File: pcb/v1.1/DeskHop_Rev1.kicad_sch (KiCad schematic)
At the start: 20 parts, among them J1 Keyboard In, J2 Debug2, J3 Debug1, J4 Mouse In, U2 Pico Primary Custom, U3 TPD4E1U06DBVR, U4 ADuM1201BR, U5 TPD4E1U06DBVR, U6 Pico Primary Custom

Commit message: ver OneXeroOne
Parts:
- removed J2: Debug2, Connector_PinHeader_2.54mm:PinHeader_1x03_P2.54mm_Vertical, symbol Connector_Generic:Conn_01x03
- removed J3: Debug1, Connector_PinHeader_2.54mm:PinHeader_1x03_P2.54mm_Vertical, symbol Connector_Generic:Conn_01x03
- removed U3: TPD4E1U06DBVR, Library:TPD4E1U06DBVR, symbol TPD4E1U06DBVR:TPD4E1U06DBVR
- added U1: TPD4E1U06DBVR, Customs:DBV6_TEX, symbol TPD4E1U06DBVR:TPD4E1U06DBVR
- U5: footprint Library:TPD4E1U06DBVR -> Customs:DBV6_TEX
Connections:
- net GND is gone; now on net GND2: H1.1
- net GND1: now also H2.1
- net GND2: now also U1.2 (GND); no longer H2.1
- net OA+: now also U1.1 (D1+), U1.3 (D2+)
- net OA-: now also U1.4 (D2-), U1.6 (D1-)
- net UART A RX: now also U6.14 (GPIO12); no longer U6.18 (GPIO15)
- net UART A TX: now also U6.13 (GPIO11); no longer U6.17 (GPIO14)
- net UART B RX: now also U2.27 (GPIO24); no longer U2.22 (GPIO19)
- net UART B TX: now also U2.26 (GPIO23); no longer U2.21 (GPIO18)

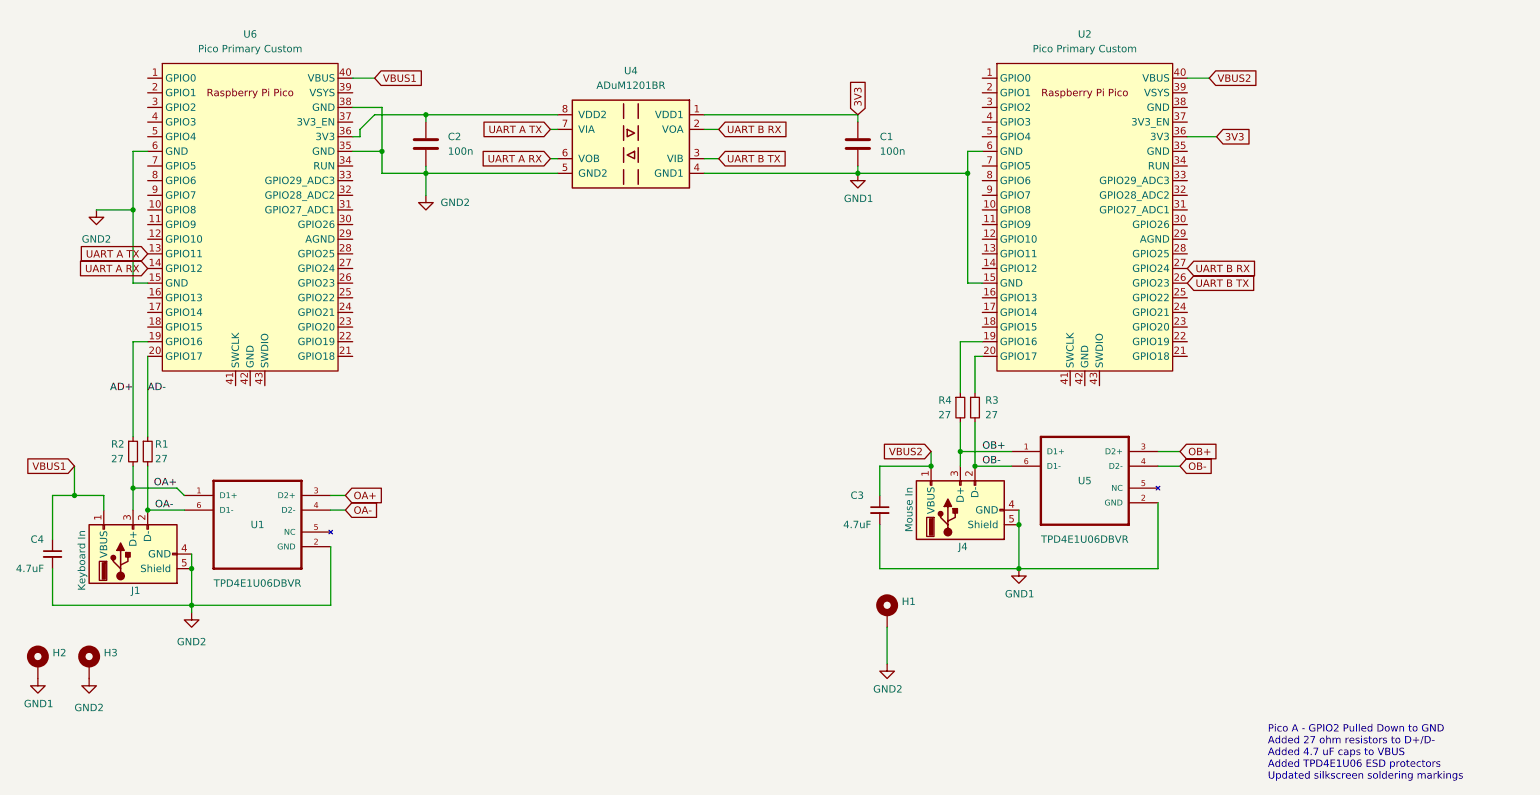
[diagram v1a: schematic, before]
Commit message: match pins to original board
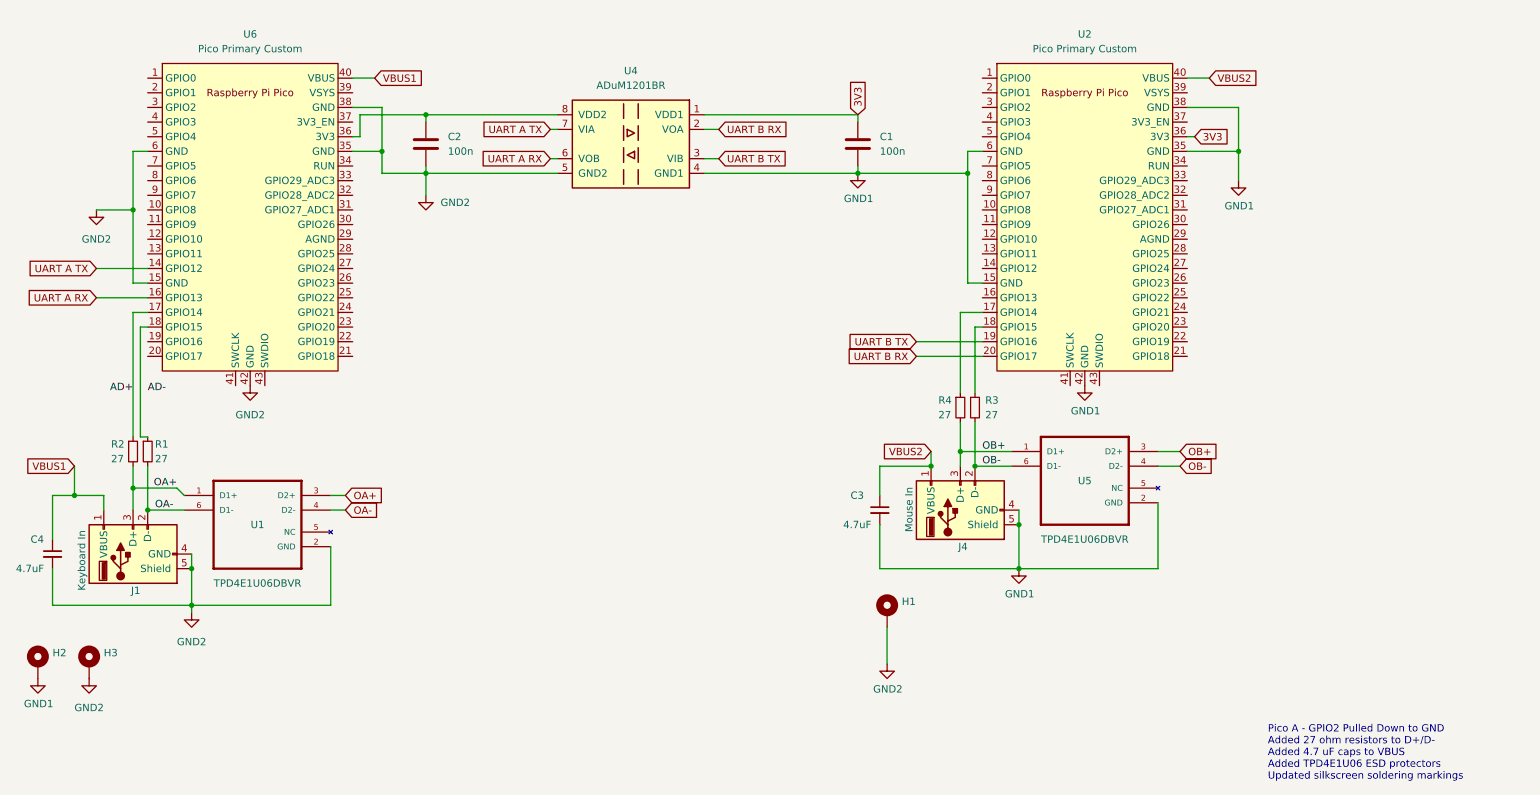
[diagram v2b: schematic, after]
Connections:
- net AD+: now also U6.17 (GPIO14); no longer U6.19 (GPIO16)
- net AD-: no longer R1.1, U6.20 (GPIO17)
- net GND1: now also U2.35 (GND), U2.38 (GND), U2.42 (GND)
- net GND2: now also U6.42 (GND)
- net UART A RX: now also U6.16 (GPIO13); no longer U6.14 (GPIO12)
- net UART A TX: now also U6.14 (GPIO12); no longer U6.13 (GPIO11)
- net UART B RX: now also U2.20 (GPIO17); no longer U2.27 (GPIO24)
- net UART B TX: now also U2.19 (GPIO16); no longer U2.26 (GPIO23)
- net at U2.17 (GPIO14): now also R4.1
- net at U2.18 (GPIO15): now also R3.1
- net at U6.18 (GPIO15): now also R1.1
